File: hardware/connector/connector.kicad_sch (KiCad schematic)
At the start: 2 parts, among them J2 Autosport, J3 Goldpin

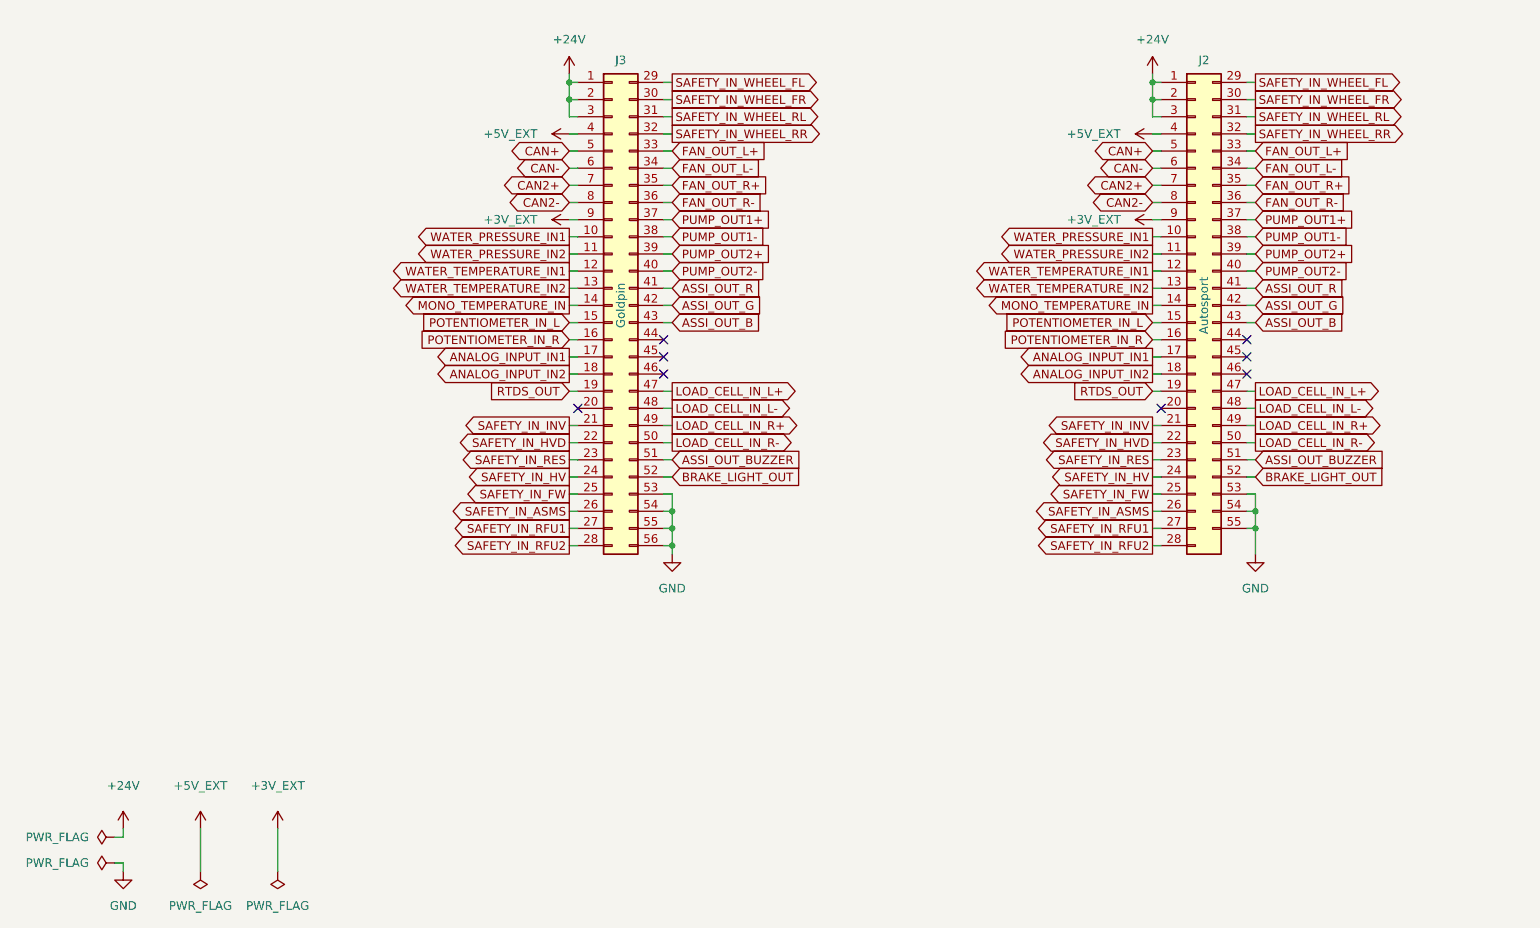
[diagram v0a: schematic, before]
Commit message: Place components on the PCB
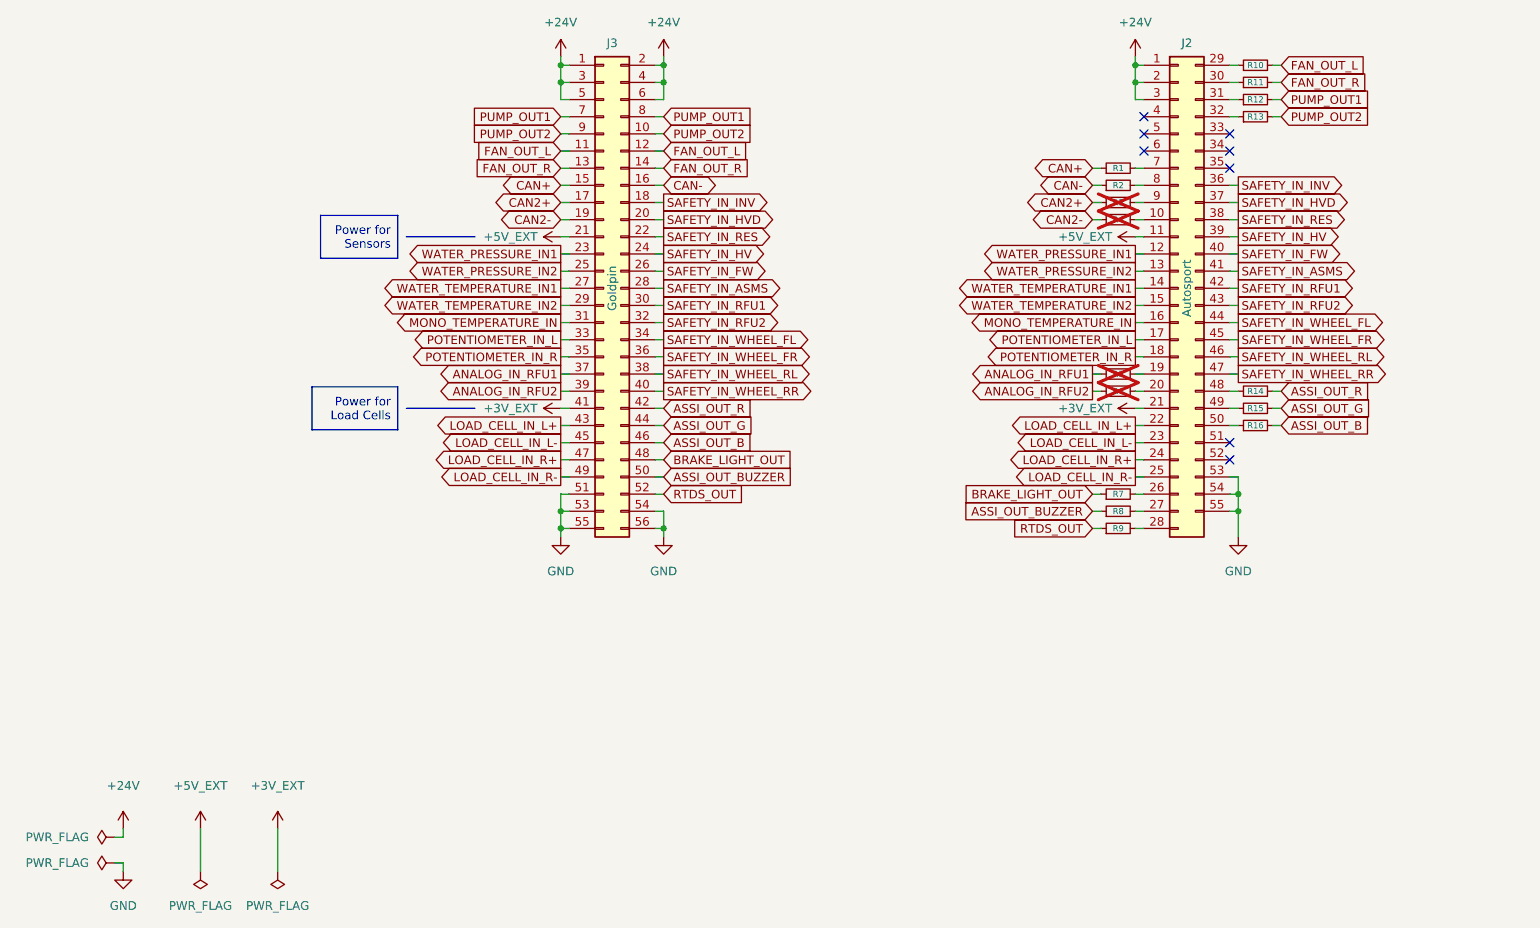
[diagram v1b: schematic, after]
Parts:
- removed J3: Goldpin, Connector_PinSocket_2.54mm:PinSocket_2x28_P2.54mm_Horizontal, symbol Connector_Generic:Conn_02x28_Top_Bottom
- added J3: Goldpin, Connector_PinHeader_2.00mm:PinHeader_2x28_P2.00mm_Horizontal, symbol Connector_Generic:Conn_02x28_Odd_Even
- added R1, R10, R11, R12, R13, R14, R15, R16, R2, R3, R4, R5, R6, R7, R8, R9: 0R, Resistor_SMD:R_0603_1608Metric, symbol Device:R_Small
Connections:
- net ANALOG_INPUT_IN1 is gone; now on net POTENTIOMETER_IN_L: J2.17 (Pin_17)
- net ANALOG_INPUT_IN2 is gone; now on net POTENTIOMETER_IN_R: J2.18 (Pin_18)
- net FAN_OUT_R- is gone; now on net SAFETY_IN_INV: J2.36 (Pin_36)
- net PUMP_OUT1+ is gone; now on net SAFETY_IN_HVD: J2.37 (Pin_37)
- net PUMP_OUT1- is gone; now on net SAFETY_IN_RES: J2.38 (Pin_38)
- net PUMP_OUT2+ is gone; now on net SAFETY_IN_HV: J2.39 (Pin_39)
- net PUMP_OUT2- is gone; now on net SAFETY_IN_FW: J2.40 (Pin_40)
- net +24V: now also J3.1 (Pin_1), J3.2 (Pin_2), J3.3 (Pin_3), J3.4 (Pin_4), J3.5 (Pin_5), J3.6 (Pin_6)
- net +3V_EXT: now also J2.21 (Pin_21), J3.41 (Pin_41); no longer J2.9 (Pin_9)
- net +5V_EXT: now also J2.11 (Pin_11), J3.21 (Pin_21); no longer J2.4 (Pin_4)
- net ASSI_OUT_B: now also J3.46 (Pin_46), R16.2; no longer J2.43 (Pin_43)
- net ASSI_OUT_BUZZER: now also J3.50 (Pin_50), R8.1; no longer J2.51 (Pin_51)
- net ASSI_OUT_G: now also J3.44 (Pin_44), R15.2; no longer J2.42 (Pin_42)
- net ASSI_OUT_R: now also J3.42 (Pin_42), R14.2; no longer J2.41 (Pin_41)
- net BRAKE_LIGHT_OUT: now also J3.48 (Pin_48), R7.1; no longer J2.52 (Pin_52)
- net CAN+: now also J3.15 (Pin_15), R1.1; no longer J2.5 (Pin_5)
- net CAN-: now also J3.16 (Pin_16), R2.1; no longer J2.6 (Pin_6)
- net CAN2+: now also J3.17 (Pin_17), R3.1; no longer J2.7 (Pin_7)
- net CAN2-: now also J3.19 (Pin_19), R4.1; no longer J2.8 (Pin_8)
- net GND: now also J3.51 (Pin_51), J3.53 (Pin_53), J3.54 (Pin_54), J3.55 (Pin_55), J3.56 (Pin_56)
- net LOAD_CELL_IN_L+: now also J2.22 (Pin_22), J3.43 (Pin_43); no longer J2.47 (Pin_47)
- net LOAD_CELL_IN_L-: now also J2.23 (Pin_23), J3.45 (Pin_45); no longer J2.48 (Pin_48)
- net LOAD_CELL_IN_R+: now also J2.24 (Pin_24), J3.47 (Pin_47); no longer J2.49 (Pin_49)
- net LOAD_CELL_IN_R-: now also J2.25 (Pin_25), J3.49 (Pin_49); no longer J2.50 (Pin_50)
- net MONO_TEMPERATURE_IN: now also J2.16 (Pin_16), J3.31 (Pin_31); no longer J2.14 (Pin_14)
- net POTENTIOMETER_IN_L: now also J3.33 (Pin_33); no longer J2.15 (Pin_15)
- net POTENTIOMETER_IN_R: now also J3.35 (Pin_35); no longer J2.16 (Pin_16)
- net RTDS_OUT: now also J3.52 (Pin_52), R9.1; no longer J2.19 (Pin_19)
- net SAFETY_IN_ASMS: now also J2.41 (Pin_41), J3.28 (Pin_28); no longer J2.26 (Pin_26)
- net SAFETY_IN_FW: now also J3.26 (Pin_26); no longer J2.25 (Pin_25)
- net SAFETY_IN_HV: now also J3.24 (Pin_24); no longer J2.24 (Pin_24)
- net SAFETY_IN_HVD: now also J3.20 (Pin_20); no longer J2.22 (Pin_22)
- net SAFETY_IN_INV: now also J3.18 (Pin_18); no longer J2.21 (Pin_21)
- net SAFETY_IN_RES: now also J3.22 (Pin_22); no longer J2.23 (Pin_23)
- net SAFETY_IN_RFU1: now also J2.42 (Pin_42), J3.30 (Pin_30); no longer J2.27 (Pin_27)
- net SAFETY_IN_RFU2: now also J2.43 (Pin_43), J3.32 (Pin_32); no longer J2.28 (Pin_28)
- net SAFETY_IN_WHEEL_FL: now also J2.44 (Pin_44), J3.34 (Pin_34); no longer J2.29 (Pin_29)
- net SAFETY_IN_WHEEL_FR: now also J2.45 (Pin_45), J3.36 (Pin_36); no longer J2.30 (Pin_30)
- net SAFETY_IN_WHEEL_RL: now also J2.46 (Pin_46), J3.38 (Pin_38); no longer J2.31 (Pin_31)
- net SAFETY_IN_WHEEL_RR: now also J2.47 (Pin_47), J3.40 (Pin_40); no longer J2.32 (Pin_32)
- net WATER_PRESSURE_IN1: now also J2.12 (Pin_12), J3.23 (Pin_23); no longer J2.10 (Pin_10)
- net WATER_PRESSURE_IN2: now also J2.13 (Pin_13), J3.25 (Pin_25); no longer J2.11 (Pin_11)
- net WATER_TEMPERATURE_IN1: now also J2.14 (Pin_14), J3.27 (Pin_27); no longer J2.12 (Pin_12)
- net WATER_TEMPERATURE_IN2: now also J2.15 (Pin_15), J3.29 (Pin_29); no longer J2.13 (Pin_13)
- net at J2.20 (Pin_20): now also R6.2
- net FAN_OUT_L+: no longer names the net of J2.33 (Pin_33)
- net FAN_OUT_L-: no longer names the net of J2.34 (Pin_34)
- net FAN_OUT_R+: no longer names the net of J2.35 (Pin_35)
- new net: J2.28 (Pin_28), R9.2
- new net: J2.27 (Pin_27), R8.2
- new net: J2.26 (Pin_26), R7.2
- new net: J2.31 (Pin_31), R12.1
- new net: J2.32 (Pin_32), R13.1
- new net: J2.10 (Pin_10), R4.2
- new net: J2.7 (Pin_7), R1.2
- new net: J2.30 (Pin_30), R11.1
- new net: J2.19 (Pin_19), R5.2
- new net: J2.49 (Pin_49), R15.1
- new net: J2.9 (Pin_9), R3.2
- new net: J2.8 (Pin_8), R2.2
- new net: J2.48 (Pin_48), R14.1
- new net: J2.50 (Pin_50), R16.1
- new net: J2.29 (Pin_29), R10.1
- new net ANALOG_IN_RFU1: J3.37 (Pin_37), R5.1
- new net ANALOG_IN_RFU2: J3.39 (Pin_39), R6.1
- new net FAN_OUT_L: J3.11 (Pin_11), J3.12 (Pin_12), R10.2
- new net FAN_OUT_R: J3.13 (Pin_13), J3.14 (Pin_14), R11.2
- new net PUMP_OUT1: J3.7 (Pin_7), J3.8 (Pin_8), R12.2
- new net PUMP_OUT2: J3.10 (Pin_10), J3.9 (Pin_9), R13.2
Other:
- moved on the sheet: J2

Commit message: Route PCB tracks
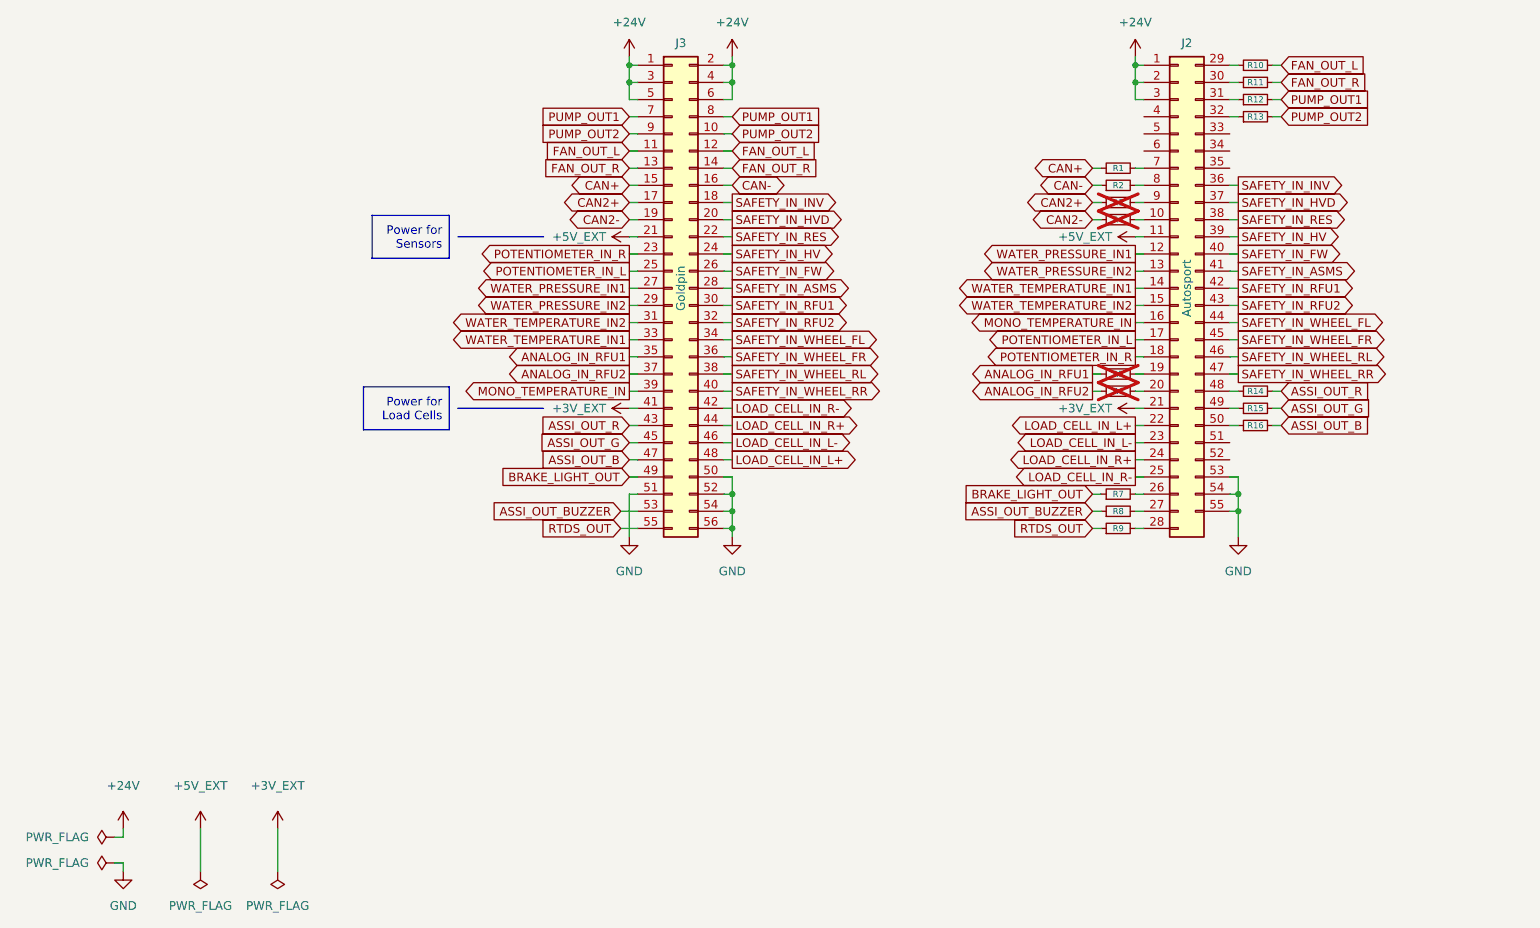
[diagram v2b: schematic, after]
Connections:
- net ANALOG_IN_RFU1: now also J3.35 (Pin_35); no longer J3.37 (Pin_37)
- net ANALOG_IN_RFU2: now also J3.37 (Pin_37); no longer J3.39 (Pin_39)
- net ASSI_OUT_B: now also J3.47 (Pin_47); no longer J3.46 (Pin_46)
- net ASSI_OUT_BUZZER: now also J3.53 (Pin_53); no longer J3.50 (Pin_50)
- net ASSI_OUT_G: now also J3.45 (Pin_45); no longer J3.44 (Pin_44)
- net ASSI_OUT_R: now also J3.43 (Pin_43); no longer J3.42 (Pin_42)
- net BRAKE_LIGHT_OUT: now also J3.49 (Pin_49); no longer J3.48 (Pin_48)
- net GND: now also J3.50 (Pin_50), J3.52 (Pin_52); no longer J3.53 (Pin_53), J3.55 (Pin_55)
- net LOAD_CELL_IN_L+: now also J3.48 (Pin_48); no longer J3.43 (Pin_43)
- net LOAD_CELL_IN_L-: now also J3.46 (Pin_46); no longer J3.45 (Pin_45)
- net LOAD_CELL_IN_R+: now also J3.44 (Pin_44); no longer J3.47 (Pin_47)
- net LOAD_CELL_IN_R-: now also J3.42 (Pin_42); no longer J3.49 (Pin_49)
- net MONO_TEMPERATURE_IN: now also J3.39 (Pin_39); no longer J3.31 (Pin_31)
- net POTENTIOMETER_IN_L: now also J3.25 (Pin_25); no longer J3.33 (Pin_33)
- net POTENTIOMETER_IN_R: now also J3.23 (Pin_23); no longer J3.35 (Pin_35)
- net RTDS_OUT: now also J3.55 (Pin_55); no longer J3.52 (Pin_52)
- net WATER_PRESSURE_IN1: now also J3.27 (Pin_27); no longer J3.23 (Pin_23)
- net WATER_PRESSURE_IN2: now also J3.29 (Pin_29); no longer J3.25 (Pin_25)
- net WATER_TEMPERATURE_IN1: now also J3.33 (Pin_33); no longer J3.27 (Pin_27)
- net WATER_TEMPERATURE_IN2: now also J3.31 (Pin_31); no longer J3.29 (Pin_29)
- no-connect marks 8 -> 0
